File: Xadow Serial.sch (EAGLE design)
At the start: 33 parts, among them J2 12p 0.5mm bottom contact, J3 12p 0.5mm bottom contact, J4 12p 0.5mm bottom contact, J5 MINI-USB-5P-3400020P1, U1 SC16IS750, U2 BSS138PS, X1 CTS_32X25_SMD

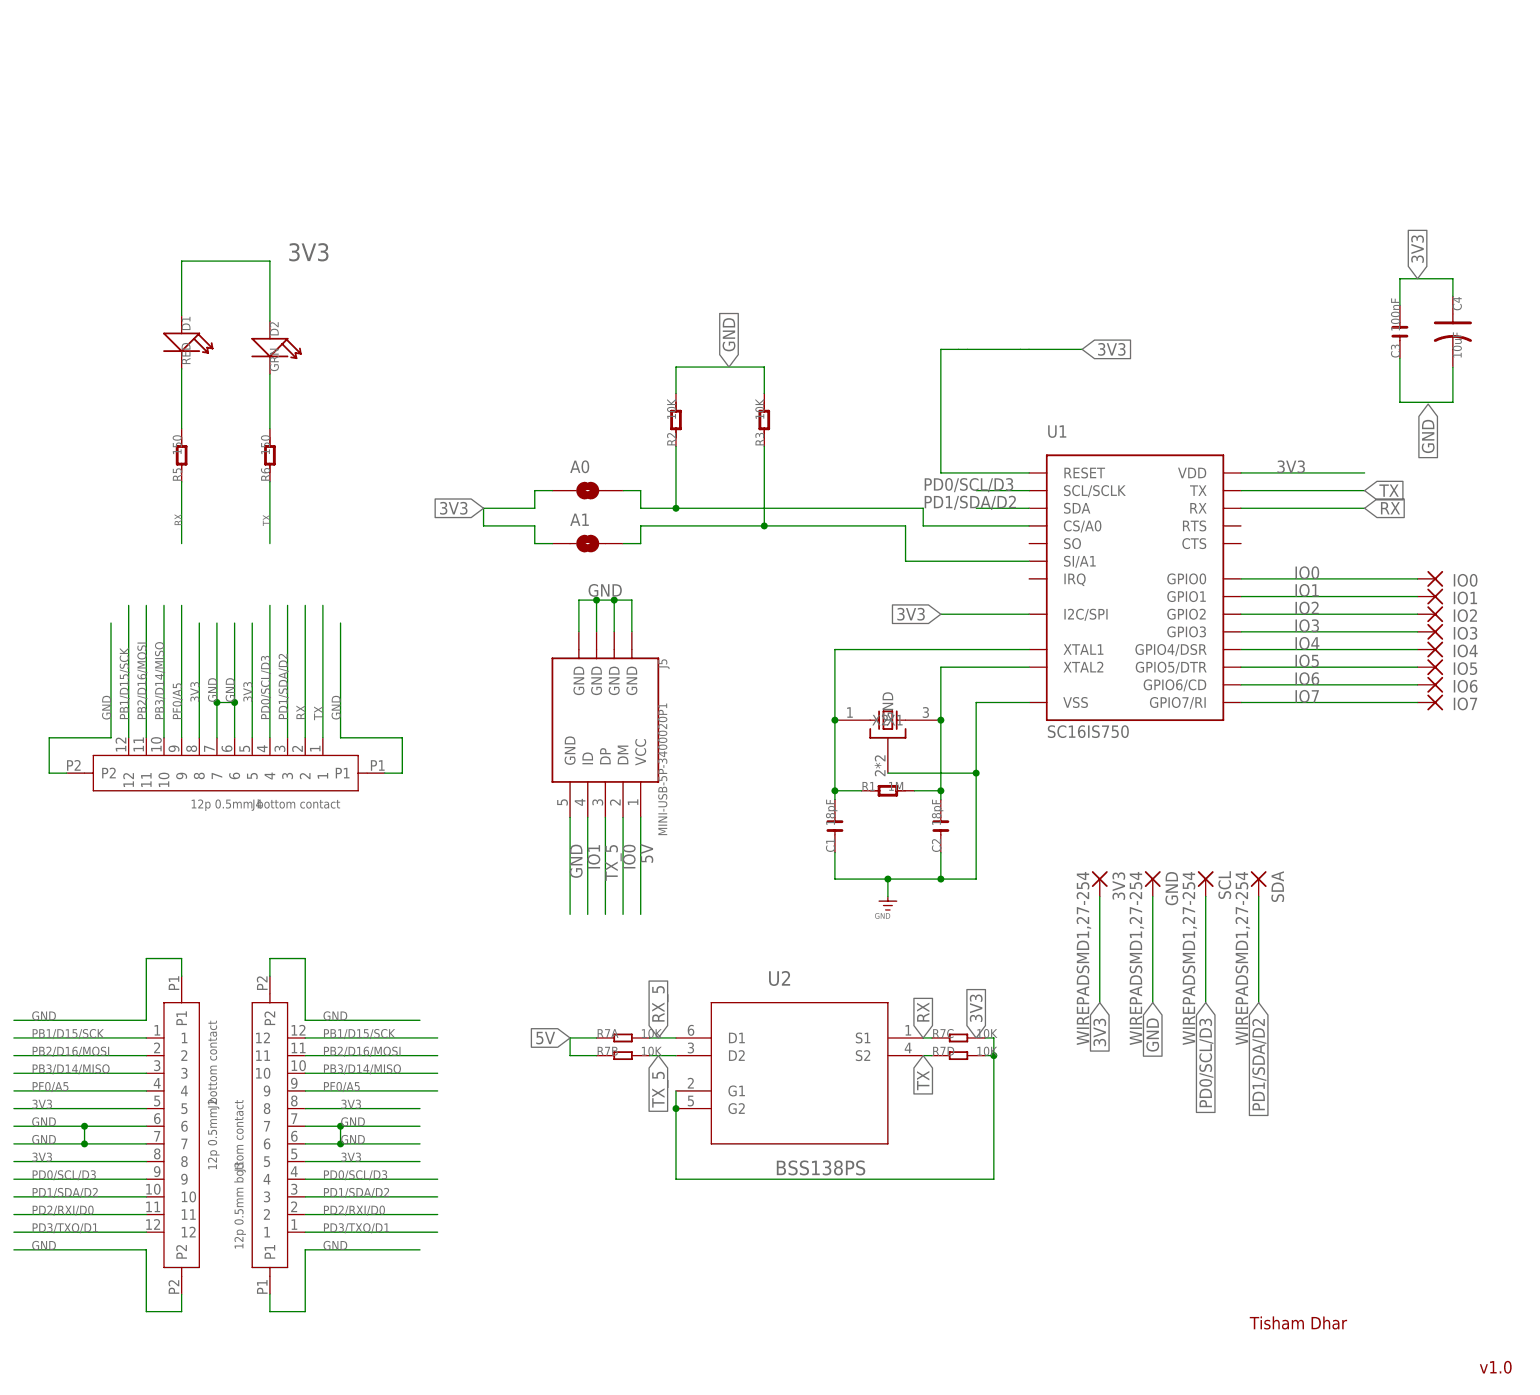
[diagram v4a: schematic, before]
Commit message: Routed to OSHPark DRU and sent for fab
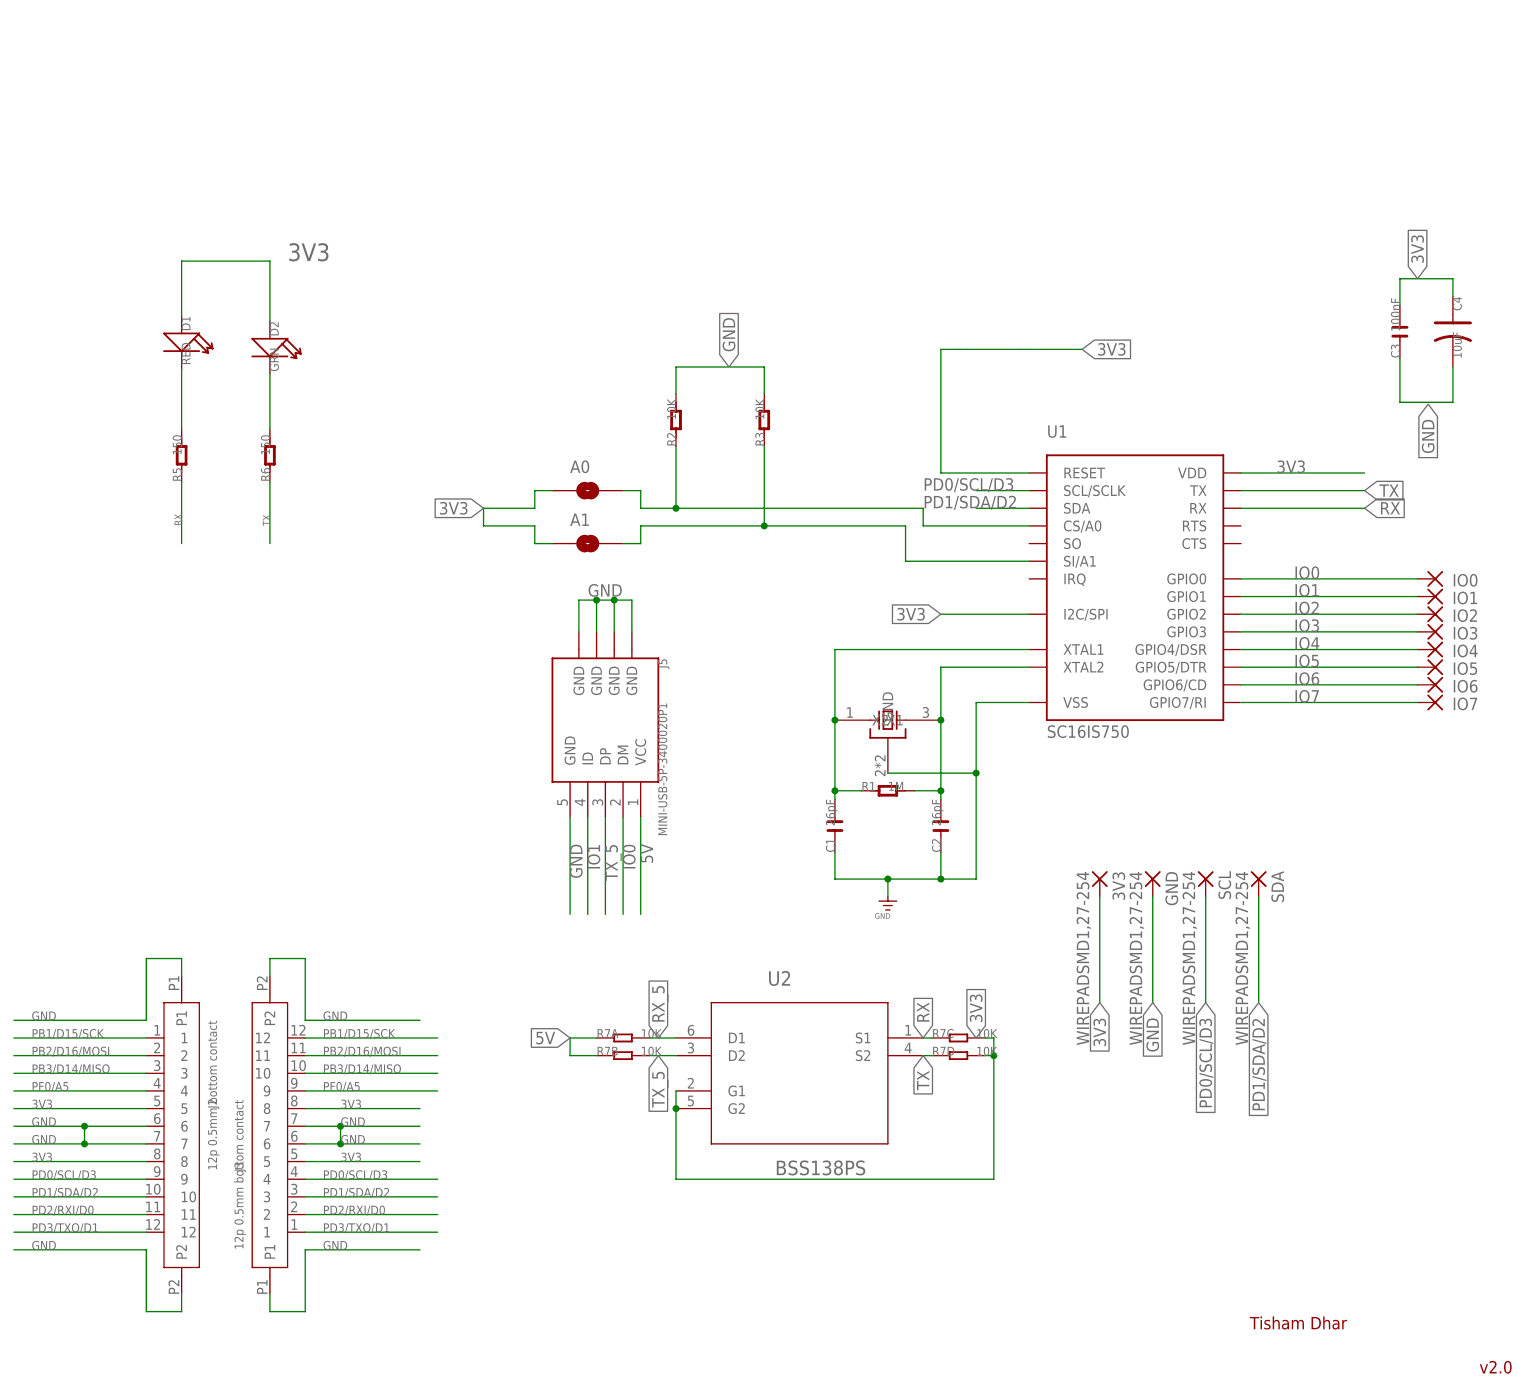
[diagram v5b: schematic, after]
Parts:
- removed J4: 12p 0.5mm bottom contact, template:FPC052002-12LT
- C1, C2: value 18pF -> 26pF
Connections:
- net 3V3: no longer J4.5, J4.8
- net GND: no longer J4.6, J4.7, J4.P1, J4.P2
- net PB1/D15/SCK: no longer J4.12
- net PB2/D16/MOSI: no longer J4.11
- net PB3/D14/MISO: no longer J4.10
- net PD0/SCL/D3: no longer J4.4
- net PD1/SDA/D2: no longer J4.3
- net PF0/A5: no longer J4.9
- net RX: no longer J4.2
- net TX: no longer J4.1
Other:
- note added: "v2.0"
- note removed: "v1.0"
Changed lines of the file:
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@@
 <part name="U1" library="nxpsemi" deviceset="SC16IS750" device=""/>
 <part name="X1" library="cts_crystal" deviceset="CTS_32X25_SMD" device=""/>
-<part name="C1" library="OPL" deviceset="C*" device="-0603" value="18pF"/>
-<part name="C2" library="OPL" deviceset="C*" device="-0603" value="18pF"/>
+<part name="C1" library="OPL" deviceset="C*" device="-0603" value="26pF"/>
+<part name="C2" library="OPL" deviceset="C*" device="-0603" value="26pF"/>
 <part name="R1" library="OPL" deviceset="R*" device="-0603" value="1M"/>
 <part name="C3" library="OPL" deviceset="C*" device="-0603" value="100nF"/>
@@
 <part name="R3" library="OPL" deviceset="R*" device="-0603" value="10K"/>
 <part name="U$5" library="Power or GND " deviceset="GND_POWER" device="" value="GND"/>
-<part name="J4" library="template" deviceset="FPC052002-12LT" device="" value="12p 0.5mm bottom contact"/>
 <part name="D1" library="OPL" deviceset="LED*" device="" value="RED"/>
 <part name="D2" library="OPL" deviceset="LED*" device="" value="GRN"/>
@@
 <plain>
 <text x="191.77" y="11.43" size="1.778" layer="94" ratio="10">Tisham Dhar</text>
-<text x="224.79" y="5.08" size="1.778" layer="94" ratio="10">v1.0</text>
+<text x="224.79" y="5.08" size="1.778" layer="94" ratio="10">v2.0</text>
 </plain>
 <instances>
@@
 <instance part="R3" gate="R" x="121.92" y="142.24" rot="R90"/>
 <instance part="U$5" gate="G$1" x="139.7" y="73.66"/>
-<instance part="J4" gate="G$1" x="44.45" y="91.44" rot="R270"/>
 <instance part="D1" gate="LED" x="38.1" y="153.416" rot="R270"/>
 <instance part="D2" gate="LED" x="50.8" y="152.654" rot="R270"/>
@@
 </segment>
 <segment>
-<wire x1="43.18" y1="96.52" x2="43.18" y2="101.6" width="0.1524" layer="91"/>
-<wire x1="43.18" y1="101.6" x2="43.18" y2="113.03" width="0.1524" layer="91"/>
-<wire x1="45.72" y1="113.03" x2="45.72" y2="101.6" width="0.1524" layer="91"/>
-<label x="43.18" y="101.6" size="1.27" layer="95" ratio="10" rot="R90"/>
-<label x="45.72" y="101.6" size="1.27" layer="95" ratio="10" rot="R90"/>
-<pinref part="J4" gate="G$1" pin="6"/>
-<pinref part="J4" gate="G$1" pin="7"/>
-<wire x1="45.72" y1="101.6" x2="45.72" y2="96.52" width="0.1524" layer="91"/>
-<wire x1="43.18" y1="101.6" x2="45.72" y2="101.6" width="0.1524" layer="91"/>
-<junction x="43.18" y="101.6"/>
-<junction x="45.72" y="101.6"/>
-</segment>
-<segment>
-<pinref part="J4" gate="G$1" pin="P2"/>
-<wire x1="19.05" y1="91.44" x2="21.59" y2="91.44" width="0.1524" layer="91"/>
-<wire x1="19.05" y1="91.44" x2="19.05" y2="96.52" width="0.1524" layer="91"/>
-<wire x1="19.05" y1="96.52" x2="27.94" y2="96.52" width="0.1524" layer="91"/>
-<wire x1="27.94" y1="96.52" x2="27.94" y2="113.03" width="0.1524" layer="91"/>
-<label x="27.94" y="99.06" size="1.27" layer="95" ratio="10" rot="R90"/>
-</segment>
-<segment>
-<wire x1="60.96" y1="96.52" x2="60.96" y2="113.03" width="0.1524" layer="91"/>
-<pinref part="J4" gate="G$1" pin="P1"/>
-<wire x1="67.31" y1="91.44" x2="69.85" y2="91.44" width="0.1524" layer="91"/>
-<wire x1="69.85" y1="91.44" x2="69.85" y2="96.52" width="0.1524" layer="91"/>
-<wire x1="69.85" y1="96.52" x2="60.96" y2="96.52" width="0.1524" layer="91"/>
-<label x="60.96" y="99.06" size="1.27" layer="95" ratio="10" rot="R90"/>
-</segment>
-<segment>
 <pinref part="GND" gate="G$1" pin="P"/>
 <wire x1="177.8" y1="73.66" x2="177.8" y2="58.42" width="0.1524" layer="91"/>
@@
 </segment>
 <segment>
-<wire x1="40.64" y1="96.52" x2="40.64" y2="113.03" width="0.1524" layer="91"/>
-<label x="40.64" y="101.6" size="1.27" layer="95" ratio="10" rot="R90"/>
-<pinref part="J4" gate="G$1" pin="8"/>
-</segment>
-<segment>
-<wire x1="48.26" y1="96.52" x2="48.26" y2="113.03" width="0.1524" layer="91"/>
-<label x="48.26" y="101.6" size="1.27" layer="95" ratio="10" rot="R90"/>
-<pinref part="J4" gate="G$1" pin="5"/>
-</segment>
-<segment>
 <wire x1="38.1" y1="157.226" x2="38.1" y2="165.1" width="0.1524" layer="91"/>
 <wire x1="38.1" y1="165.1" x2="50.8" y2="165.1" width="0.1524" layer="91"/>
@@
 <pinref part="J3" gate="G$1" pin="12"/>
 </segment>
-<segment>
-<wire x1="30.48" y1="115.57" x2="30.48" y2="96.52" width="0.1524" layer="91"/>
-<label x="30.48" y="99.06" size="1.27" layer="95" ratio="10" rot="R90"/>
-<pinref part="J4" gate="G$1" pin="12"/>
-</segment>
 </net>
 <net name="PB3/D14/MISO" class="0">
@@
 <pinref part="J3" gate="G$1" pin="10"/>
 </segment>
-<segment>
-<wire x1="35.56" y1="96.52" x2="35.56" y2="115.57" width="0.1524" layer="91"/>
-<label x="35.56" y="99.06" size="1.27" layer="95" ratio="10" rot="R90"/>
-<pinref part="J4" gate="G$1" pin="10"/>
-</segment>
 </net>
 <net name="PB2/D16/MOSI" class="0">
@@
 <pinref part="J3" gate="G$1" pin="11"/>
 </segment>
-<segment>
-<wire x1="33.02" y1="96.52" x2="33.02" y2="115.57" width="0.1524" layer="91"/>
-<label x="33.02" y="99.06" size="1.27" layer="95" ratio="10" rot="R90"/>
-<pinref part="J4" gate="G$1" pin="11"/>
-</segment>
 </net>
 <net name="PD3/TXO/D1" class="0">
@@
 <pinref part="J3" gate="G$1" pin="9"/>
 </segment>
-<segment>
-<wire x1="38.1" y1="115.57" x2="38.1" y2="96.52" width="0.1524" layer="91"/>
-<label x="38.1" y="99.06" size="1.27" layer="95" ratio="10" rot="R90"/>
-<pinref part="J4" gate="G$1" pin="9"/>
-</segment>
 </net>
 <net name="PD1/SDA/D2" class="0">
@@
 </segment>
 <segment>
-<wire x1="53.34" y1="115.57" x2="53.34" y2="96.52" width="0.1524" layer="91"/>
-<label x="53.34" y="99.06" size="1.27" layer="95" ratio="10" rot="R90"/>
-<pinref part="J4" gate="G$1" pin="3"/>
-</segment>
-<segment>
 <pinref part="SDA" gate="G$1" pin="P"/>
 <wire x1="193.04" y1="73.66" x2="193.04" y2="58.42" width="0.1524" layer="91"/>
@@
 <wire x1="160.02" y1="132.08" x2="152.4" y2="132.08" width="0.1524" layer="91"/>
 <label x="144.78" y="132.08" size="1.778" layer="95"/>
-</segment>
-<segment>
-<wire x1="50.8" y1="96.52" x2="50.8" y2="115.57" width="0.1524" layer="91"/>
-<label x="50.8" y="99.06" size="1.27" layer="95" ratio="10" rot="R90"/>
-<pinref part="J4" gate="G$1" pin="4"/>
 </segment>
 <segment>
@@
 </segment>
 <segment>
-<wire x1="55.88" y1="96.52" x2="55.88" y2="115.57" width="0.1524" layer="91"/>
-<label x="55.88" y="99.06" size="1.27" layer="95" ratio="10" rot="R90"/>
-<pinref part="J4" gate="G$1" pin="2"/>
-</segment>
-<segment>
 <label x="38.1" y="127" size="1.016" layer="95" rot="R90"/>
 <pinref part="R5" gate="R" pin="1"/>
@@
 </segment>
 <segment>
-<wire x1="58.42" y1="115.57" x2="58.42" y2="96.52" width="0.1524" layer="91"/>
-<label x="58.42" y="99.06" size="1.27" layer="95" ratio="10" rot="R90"/>
-<pinref part="J4" gate="G$1" pin="1"/>
-</segment>
-<segment>

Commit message: Converted to use SPI
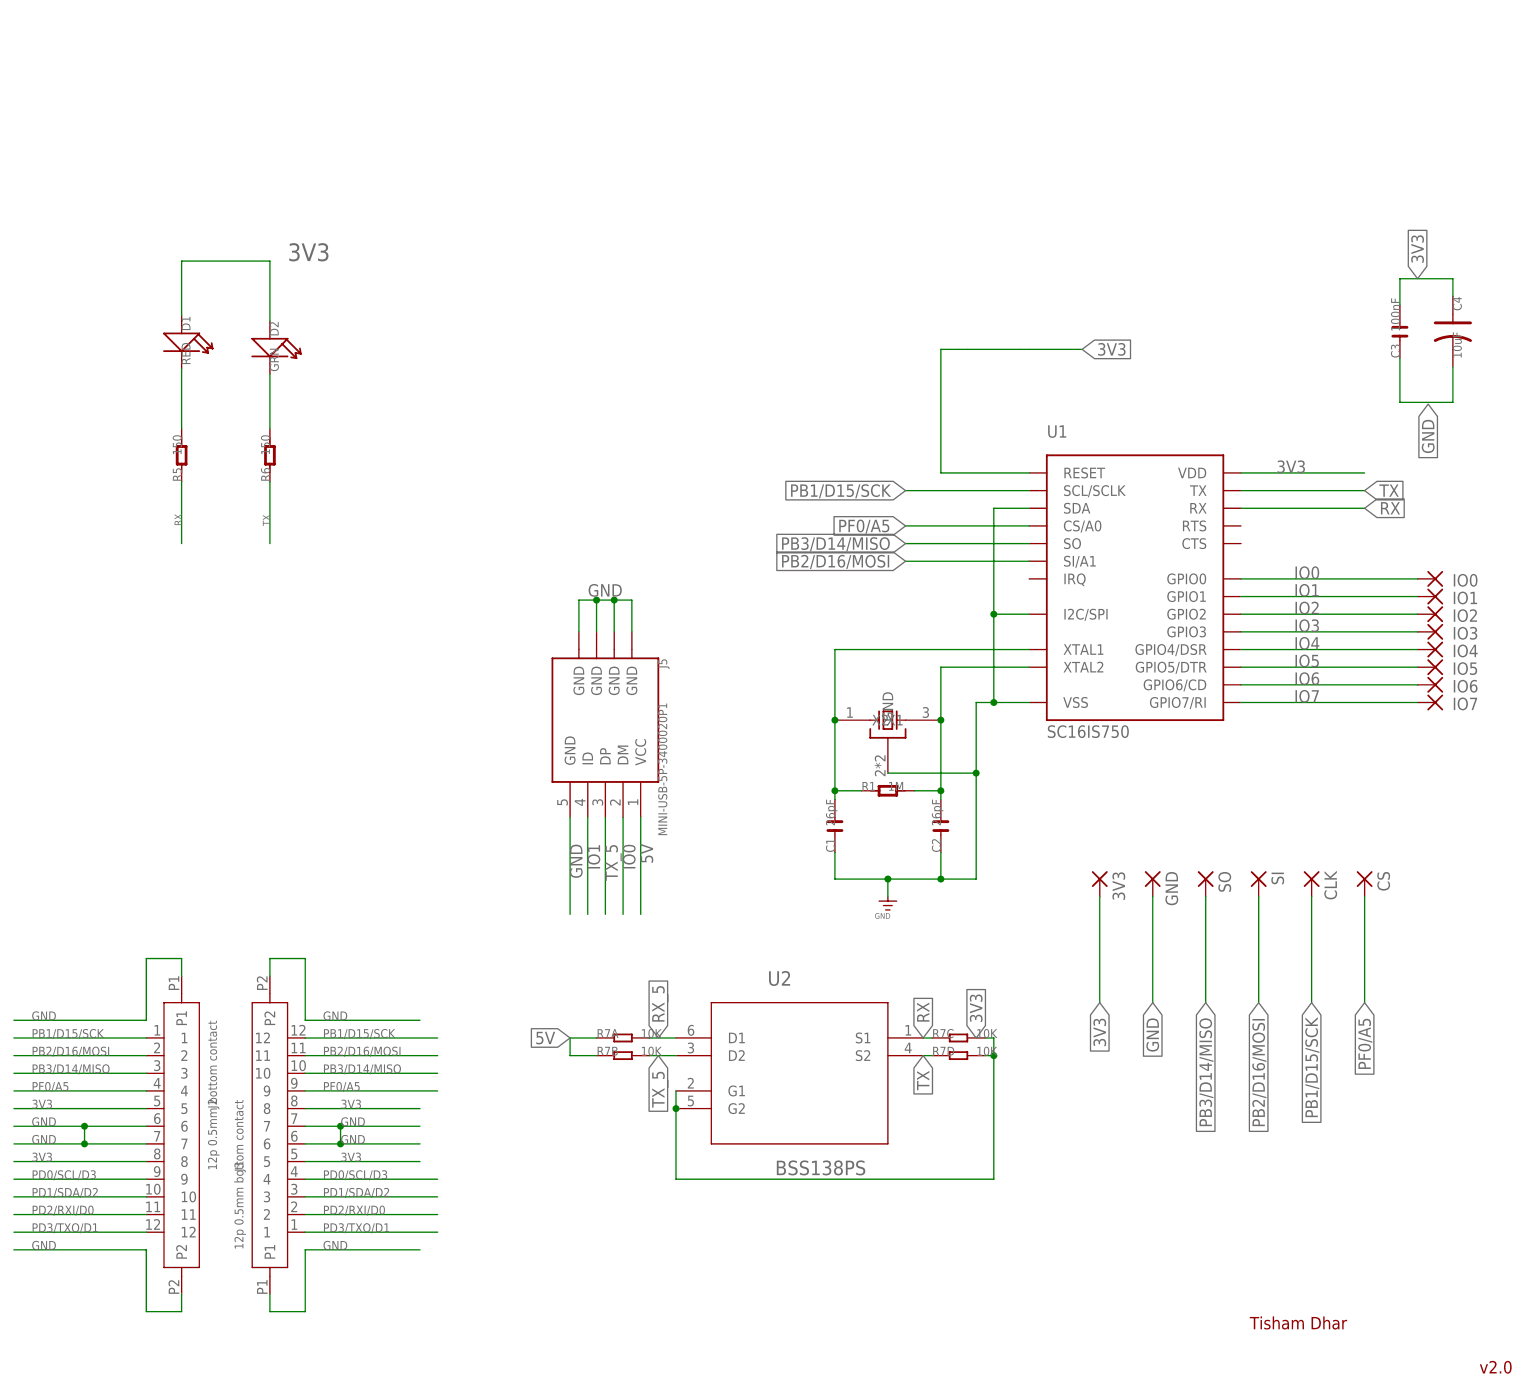
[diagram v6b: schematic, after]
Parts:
- removed A0, A1: JUMPER-PAD-2-NO, SparkFun-Passives:JUMPER-PAD-2-NO
- removed R2, R3: 10K, OPL:R-0603
- added CLK, CS: WIREPADSMD1,27-254, wirepad:WIREPADSMD1,27-254
- renumbered SCL to SO, SDA to SI
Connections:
- removed net N$3: A1.2, R3.1, U1.SI/A1
- removed net N$4: A0.2, R2.1, U1.CS/A0
- net 3V3: no longer A0.1, A1.1, U1.I2C/SPI
- net GND: now also U1.I2C/SPI, U1.SDA; no longer R2.2, R3.2
- net PB1/D15/SCK: now also CLK.P, U1.SCL/SCLK
- net PB2/D16/MOSI: now also SI.P, U1.SI/A1
- net PB3/D14/MISO: now also SO.P, U1.SO
- net PD0/SCL/D3: no longer SO.P, U1.SCL/SCLK
- net PD1/SDA/D2: no longer SI.P, U1.SDA
- net PF0/A5: now also CS.P, U1.CS/A0
